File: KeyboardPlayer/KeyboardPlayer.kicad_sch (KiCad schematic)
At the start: 16 parts, among them J1 MJ-4PP-9, J2 Conn_01x03, SW1 SW_PUSH, SW2 RotaryEncoder_Switch, SW3 SW_PUSH, SW4 SW_PUSH, SW5 RESET_SW, SW6 SW_PUSH, SW7 SW_PUSH, U1 ProMicro

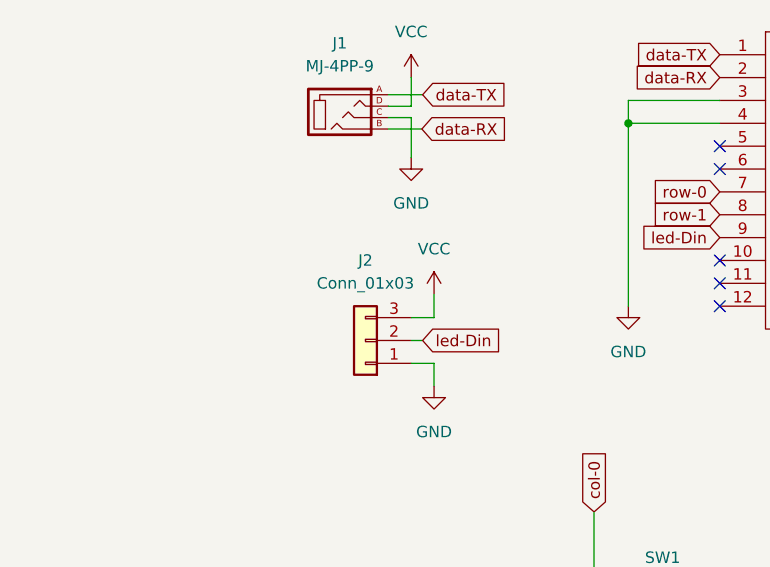
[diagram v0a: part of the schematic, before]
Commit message: assingnment footpring of parts
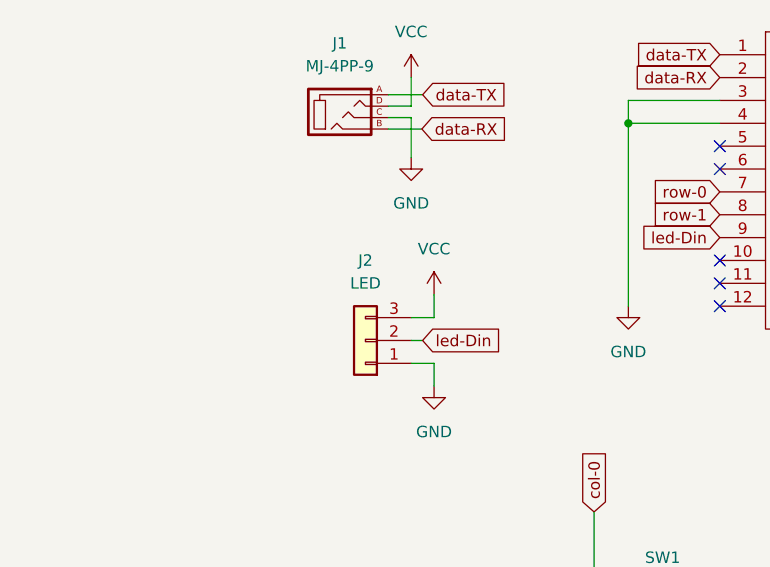
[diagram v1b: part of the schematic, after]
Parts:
- D1, D2, D3, D4, D5: footprint (none) -> kbd.pretty:D3_TH_SMD_v2
- D6: footprint (none) -> kbd.pretty:D3_TH_SMD
- J1: footprint (none) -> kbd.pretty:MJ-4PP-9
- J2: value Conn_01x03 -> LED; footprint (none) -> kbd.pretty:StripLED_rev
- SW5: footprint (none) -> kbd.pretty:ResetSW
- U1: footprint (none) -> kbd.pretty:ProMicro_v2
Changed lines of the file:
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@@
       (effects (font (size 1.27 1.27)) (justify right))
     )
-    (property "Footprint" "" (id 2) (at 116.84 105.41 0)
+    (property "Footprint" "kbd.pretty:D3_TH_SMD_v2" (id 2) (at 116.84 105.41 0)
       (effects (font (size 1.27 1.27)) hide)
     )
@@
       (effects (font (size 1.27 1.27)) (justify right))
     )
-    (property "Footprint" "" (id 2) (at 78.74 105.41 0)
+    (property "Footprint" "kbd.pretty:D3_TH_SMD_v2" (id 2) (at 78.74 105.41 0)
       (effects (font (size 1.27 1.27)) hide)
     )
@@
     (in_bom yes) (on_board yes) (fields_autoplaced)
     (property "Reference" "J2" (id 0) (at 38.1 60.96 0))
-    (property "Value" "Conn_01x03" (id 1) (at 38.1 63.5 0))
-    (property "Footprint" "" (id 2) (at 38.1 69.85 0)
+    (property "Value" "LED" (id 1) (at 38.1 63.5 0))
+    (property "Footprint" "kbd.pretty:StripLED_rev" (id 2) (at 38.1 69.85 0)
       (effects (font (size 1.27 1.27)) hide)
     )
@@
     (property "Reference" "SW4" (id 0) (at 109.22 130.81 0))
     (property "Value" "SW_PUSH" (id 1) (at 109.22 133.35 0))
-    (property "Footprint" "" (id 2) (at 109.22 138.43 0))
+    (property "Footprint" "" (id 2) (at 109.22 138.43 0)
+      (effects (font (size 1.27 1.27)) hide)
+    )
     (property "Datasheet" "" (id 3) (at 109.22 138.43 0))
     (pin "1")
@@
     (property "Reference" "SW7" (id 0) (at 147.32 130.81 0))
     (property "Value" "SW_PUSH" (id 1) (at 147.32 133.35 0))
-    (property "Footprint" "" (id 2) (at 147.32 138.43 0))
+    (property "Footprint" "" (id 2) (at 147.32 138.43 0)
+      (effects (font (size 1.27 1.27)) hide)
+    )
     (property "Datasheet" "" (id 3) (at 147.32 138.43 0))
     (pin "1")
@@
     (property "Reference" "J1" (id 0) (at 35.2425 36.83 0))
     (property "Value" "MJ-4PP-9" (id 1) (at 35.2425 39.37 0))
-    (property "Footprint" "" (id 2) (at 42.545 40.005 0)
+    (property "Footprint" "kbd.pretty:MJ-4PP-9" (id 2) (at 42.545 40.005 0)
       (effects (font (size 1.27 1.27)) hide)
     )
@@
     (property "Reference" "SW5" (id 0) (at 144.78 36.83 0))
     (property "Value" "RESET_SW" (id 1) (at 144.78 39.37 0))
-    (property "Footprint" "" (id 2) (at 144.78 44.45 0))
+    (property "Footprint" "kbd.pretty:ResetSW" (id 2) (at 144.78 44.45 0)
+      (effects (font (size 1.27 1.27)) hide)
+    )
     (property "Datasheet" "" (id 3) (at 144.78 44.45 0))
     (pin "1")
@@
       (effects (font (size 1.27 1.27)) (justify right))
     )
-    (property "Footprint" "" (id 2) (at 154.94 105.41 0)
+    (property "Footprint" "kbd.pretty:D3_TH_SMD_v2" (id 2) (at 154.94 105.41 0)
       (effects (font (size 1.27 1.27)) hide)
     )
@@
     (property "Reference" "SW3" (id 0) (at 109.22 93.98 0))
     (property "Value" "SW_PUSH" (id 1) (at 109.22 96.52 0))
-    (property "Footprint" "" (id 2) (at 109.22 101.6 0))
+    (property "Footprint" "" (id 2) (at 109.22 101.6 0)
+      (effects (font (size 1.27 1.27)) hide)
+    )
     (property "Datasheet" "" (id 3) (at 109.22 101.6 0))
     (pin "1")
@@
       (effects (font (size 1.524 1.524)))
     )
-    (property "Footprint" "" (id 2) (at 97.79 78.74 0)
-      (effects (font (size 1.524 1.524)))
+    (property "Footprint" "kbd.pretty:ProMicro_v2" (id 2) (at 97.79 78.74 0)
+      (effects (font (size 1.524 1.524)) hide)
     )
     (property "Datasheet" "" (id 3) (at 97.79 78.74 0)
@@
     (property "Reference" "SW6" (id 0) (at 147.32 93.98 0))
     (property "Value" "SW_PUSH" (id 1) (at 147.32 96.52 0))
-    (property "Footprint" "" (id 2) (at 147.32 101.6 0))
+    (property "Footprint" "" (id 2) (at 147.32 101.6 0)
+      (effects (font (size 1.27 1.27)) hide)
+    )
     (property "Datasheet" "" (id 3) (at 147.32 101.6 0))
     (pin "1")
@@
       (effects (font (size 1.27 1.27)) (justify right))
     )
-    (property "Footprint" "" (id 2) (at 116.84 142.24 0)
+    (property "Footprint" "kbd.pretty:D3_TH_SMD_v2" (id 2) (at 116.84 142.24 0)
       (effects (font (size 1.27 1.27)) hide)
     )
@@
       (effects (font (size 1.27 1.27)) (justify right))
     )
-    (property "Footprint" "" (id 2) (at 154.94 142.24 0)
+    (property "Footprint" "kbd.pretty:D3_TH_SMD" (id 2) (at 154.94 142.24 0)
       (effects (font (size 1.27 1.27)) hide)
     )
@@
     (property "Reference" "SW1" (id 0) (at 71.12 93.98 0))
     (property "Value" "SW_PUSH" (id 1) (at 71.12 96.52 0))
-    (property "Footprint" "" (id 2) (at 71.12 101.6 0))
+    (property "Footprint" "" (id 2) (at 71.12 101.6 0)
+      (effects (font (size 1.27 1.27)) hide)
+    )
     (property "Datasheet" "" (id 3) (at 71.12 101.6 0))
     (pin "1")
@@
       (effects (font (size 1.27 1.27)) (justify right))
     )
-    (property "Footprint" "" (id 2) (at 78.74 142.24 0)
+    (property "Footprint" "kbd.pretty:D3_TH_SMD_v2" (id 2) (at 78.74 142.24 0)
       (effects (font (size 1.27 1.27)) hide)
     )
@@
     )
     (path "/098225e4-d91d-4625-a1f1-4da5feb1279e"
-      (reference "D1") (unit 1) (value "D") (footprint "")
+      (reference "D1") (unit 1) (value "D") (footprint "kbd.pretty:D3_TH_SMD_v2")
     )
     (path "/dbe9ba05-a46a-4c2e-a2a8-3bab06ab2de7"
-      (reference "D2") (unit 1) (value "D") (footprint "")
+      (reference "D2") (unit 1) (value "D") (footprint "kbd.pretty:D3_TH_SMD_v2")
     )
     (path "/02ec95bc-9b18-4028-a83d-b583d5fdd405"
-      (reference "D3") (unit 1) (value "D") (footprint "")
+      (reference "D3") (unit 1) (value "D") (footprint "kbd.pretty:D3_TH_SMD_v2")
     )
     (path "/aa8a1b52-aefe-4354-a15a-1a02a835abd4"
-      (reference "D4") (unit 1) (value "D") (footprint "")
+      (reference "D4") (unit 1) (value "D") (footprint "kbd.pretty:D3_TH_SMD_v2")
     )
     (path "/8c318120-88bf-40b3-9ae9-845435ab18ae"
-      (reference "D5") (unit 1) (value "D") (footprint "")
+      (reference "D5") (unit 1) (value "D") (footprint "kbd.pretty:D3_TH_SMD_v2")
     )
     (path "/b51339ed-2880-4ea0-95e9-b26265100fe4"
-      (reference "D6") (unit 1) (value "D") (footprint "")
+      (reference "D6") (unit 1) (value "D") (footprint "kbd.pretty:D3_TH_SMD")
     )
     (path "/64218c02-0ded-4c54-b8b1-64f5986081d4"
-      (reference "J1") (unit 1) (value "MJ-4PP-9") (footprint "")
+      (reference "J1") (unit 1) (value "MJ-4PP-9") (footprint "kbd.pretty:MJ-4PP-9")
     )
     (path "/24870c24-59c6-4bc7-9100-a28c20f75746"
-      (reference "J2") (unit 1) (value "Conn_01x03") (footprint "")
+      (reference "J2") (unit 1) (value "LED") (footprint "kbd.pretty:StripLED_rev")
     )
     (path "/dae4c746-5c25-4fd0-9787-e00e0cc3e6ce"
@@
     )
     (path "/786c0e24-1cf9-498c-861d-31c3a15e2179"
-      (reference "SW5") (unit 1) (value "RESET_SW") (footprint "")
+      (reference "SW5") (unit 1) (value "RESET_SW") (footprint "kbd.pretty:ResetSW")
     )
     (path "/a2b40179-12d4-4546-85e7-fd0245d60955"
@@
     )
     (path "/97cd50c7-888e-4083-a161-c56ad1198589"
-      (reference "U1") (unit 1) (value "ProMicro") (footprint "")
-    )
-  )
+      (reference "U1") (unit 1) (value "ProMicro") (footprint "kbd.pretty:ProMicro_v2")
+    )
+  )

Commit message: assingnment footpring of parts
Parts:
- SW1, SW3, SW4, SW6, SW7: footprint (none) -> kbd.pretty:CherryMX_Choc_Hotswap
- SW2: footprint (none) -> Keebio-Parts.pretty:RotaryEncoder_EC11
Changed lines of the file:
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@@
     (property "Reference" "SW4" (id 0) (at 109.22 130.81 0))
     (property "Value" "SW_PUSH" (id 1) (at 109.22 133.35 0))
-    (property "Footprint" "" (id 2) (at 109.22 138.43 0)
+    (property "Footprint" "kbd.pretty:CherryMX_Choc_Hotswap" (id 2) (at 109.22 138.43 0)
       (effects (font (size 1.27 1.27)) hide)
     )
@@
     (property "Reference" "SW7" (id 0) (at 147.32 130.81 0))
     (property "Value" "SW_PUSH" (id 1) (at 147.32 133.35 0))
-    (property "Footprint" "" (id 2) (at 147.32 138.43 0)
+    (property "Footprint" "kbd.pretty:CherryMX_Choc_Hotswap" (id 2) (at 147.32 138.43 0)
       (effects (font (size 1.27 1.27)) hide)
     )
@@
       (effects (font (size 1.27 1.27)) (justify left))
     )
-    (property "Footprint" "" (id 2) (at 75.184 127 0)
+    (property "Footprint" "Keebio-Parts.pretty:RotaryEncoder_EC11" (id 2) (at 75.184 127 0)
       (effects (font (size 1.27 1.27)) hide)
     )
@@
     (property "Reference" "SW3" (id 0) (at 109.22 93.98 0))
     (property "Value" "SW_PUSH" (id 1) (at 109.22 96.52 0))
-    (property "Footprint" "" (id 2) (at 109.22 101.6 0)
+    (property "Footprint" "kbd.pretty:CherryMX_Choc_Hotswap" (id 2) (at 109.22 101.6 0)
       (effects (font (size 1.27 1.27)) hide)
     )
@@
     (property "Reference" "SW6" (id 0) (at 147.32 93.98 0))
     (property "Value" "SW_PUSH" (id 1) (at 147.32 96.52 0))
-    (property "Footprint" "" (id 2) (at 147.32 101.6 0)
+    (property "Footprint" "kbd.pretty:CherryMX_Choc_Hotswap" (id 2) (at 147.32 101.6 0)
       (effects (font (size 1.27 1.27)) hide)
     )
@@
     (property "Reference" "SW1" (id 0) (at 71.12 93.98 0))
     (property "Value" "SW_PUSH" (id 1) (at 71.12 96.52 0))
-    (property "Footprint" "" (id 2) (at 71.12 101.6 0)
+    (property "Footprint" "kbd.pretty:CherryMX_Choc_Hotswap" (id 2) (at 71.12 101.6 0)
       (effects (font (size 1.27 1.27)) hide)
     )
@@
     )
     (path "/dae4c746-5c25-4fd0-9787-e00e0cc3e6ce"
-      (reference "SW1") (unit 1) (value "SW_PUSH") (footprint "")
+      (reference "SW1") (unit 1) (value "SW_PUSH") (footprint "kbd.pretty:CherryMX_Choc_Hotswap")
     )
     (path "/4a1a3f2c-dafc-4657-8855-939cf0cc192d"
-      (reference "SW2") (unit 1) (value "RotaryEncoder_Switch") (footprint "")
+      (reference "SW2") (unit 1) (value "RotaryEncoder_Switch") (footprint "Keebio-Parts.pretty:RotaryEncoder_EC11")
     )
     (path "/944cee2e-48a1-4ef4-8f30-090996d47d14"
-      (reference "SW3") (unit 1) (value "SW_PUSH") (footprint "")
+      (reference "SW3") (unit 1) (value "SW_PUSH") (footprint "kbd.pretty:CherryMX_Choc_Hotswap")
     )
     (path "/330558a8-2907-43f0-96f5-3d96b9505623"
-      (reference "SW4") (unit 1) (value "SW_PUSH") (footprint "")
+      (reference "SW4") (unit 1) (value "SW_PUSH") (footprint "kbd.pretty:CherryMX_Choc_Hotswap")
     )
     (path "/786c0e24-1cf9-498c-861d-31c3a15e2179"
@@
     )
     (path "/a2b40179-12d4-4546-85e7-fd0245d60955"
-      (reference "SW6") (unit 1) (value "SW_PUSH") (footprint "")
+      (reference "SW6") (unit 1) (value "SW_PUSH") (footprint "kbd.pretty:CherryMX_Choc_Hotswap")
     )
     (path "/492235c0-bc3f-44ed-a231-610717ae900d"
-      (reference "SW7") (unit 1) (value "SW_PUSH") (footprint "")
+      (reference "SW7") (unit 1) (value "SW_PUSH") (footprint "kbd.pretty:CherryMX_Choc_Hotswap")
     )
     (path "/97cd50c7-888e-4083-a161-c56ad1198589"

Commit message: complete DRC
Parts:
- D6: footprint kbd.pretty:D3_TH_SMD -> kbd.pretty:D3_TH_SMD_v2
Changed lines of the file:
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@@
       (effects (font (size 1.27 1.27)) (justify right))
     )
-    (property "Footprint" "kbd.pretty:D3_TH_SMD" (id 2) (at 154.94 142.24 0)
+    (property "Footprint" "kbd.pretty:D3_TH_SMD_v2" (id 2) (at 154.94 142.24 0)
       (effects (font (size 1.27 1.27)) hide)
     )
@@
     )
     (path "/b51339ed-2880-4ea0-95e9-b26265100fe4"
-      (reference "D6") (unit 1) (value "D") (footprint "kbd.pretty:D3_TH_SMD")
+      (reference "D6") (unit 1) (value "D") (footprint "kbd.pretty:D3_TH_SMD_v2")
     )
     (path "/64218c02-0ded-4c54-b8b1-64f5986081d4"
